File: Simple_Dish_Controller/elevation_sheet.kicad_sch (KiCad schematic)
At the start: 19 parts, among them J2 DA15_Socket, J4 CRJ022-G-TH, Q1 PZT2222A, Q2 PZT2222A, SW2 SW_SPDT_312, U2 74LS08, U3 74LS32, U4 ICM7555xP

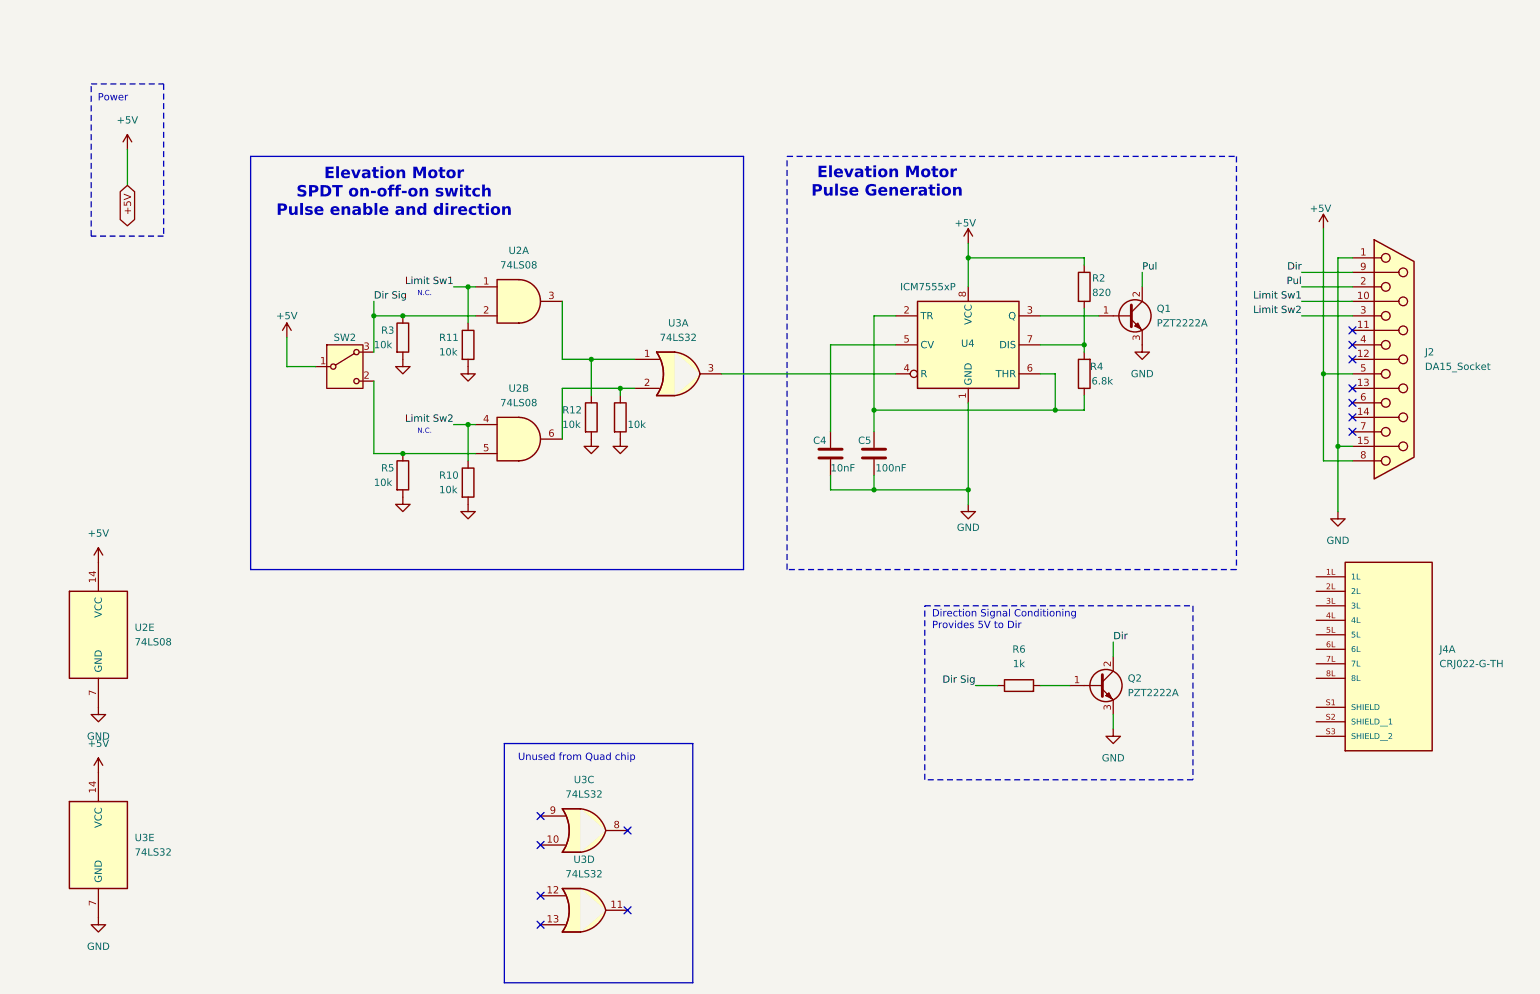
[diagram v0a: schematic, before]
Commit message: Added RJ45 ports
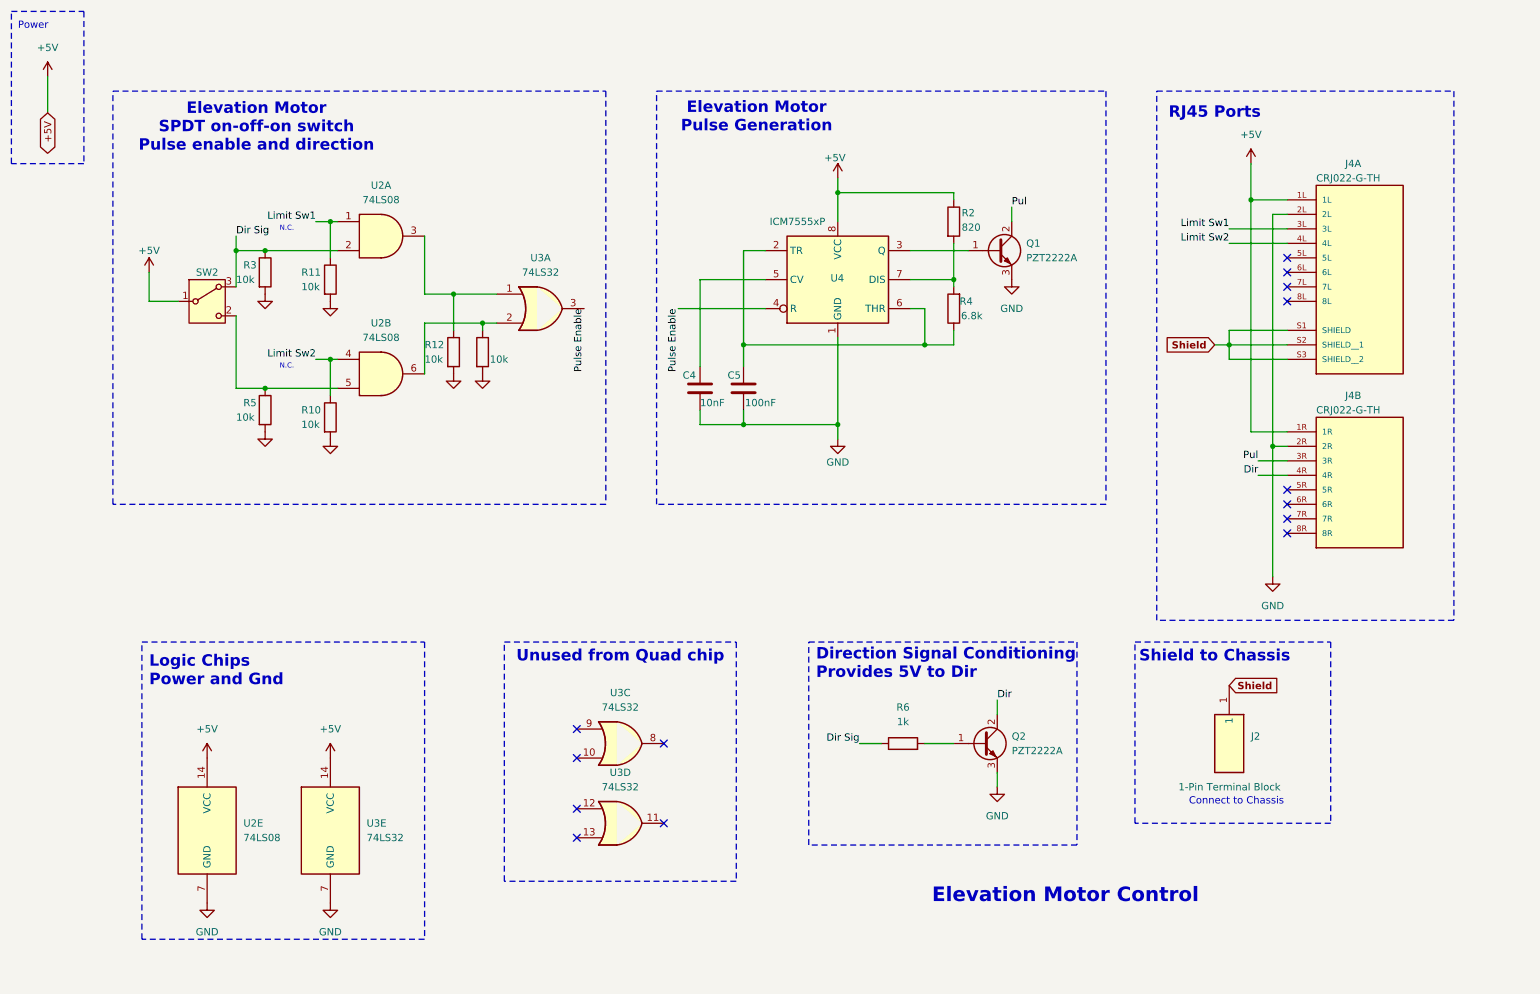
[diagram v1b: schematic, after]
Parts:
- removed J2: DA15_Socket, Connector_Dsub:DSUB-15_Socket_Horizontal_P2.77x2.54mm_EdgePinOffset9.40mm, symbol Connector:DA15_Socket
- added J2: 1-Pin Terminal Block, RHDR1W160P0X826_1X1_1020X1270X1270P, symbol 1-Pin Barrier Terminal Block:38700-6301
- added unit 2 of J4
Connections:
- net +5V: now also J4.1L, J4.1R
- net Dir: now also J4.4R
- net GND: now also J4.2L, J4.2R
- net Limit Sw1: now also J4.3L
- net Limit Sw2: now also J4.4L
- net Pul: now also J4.3R
- net Pulse Enable: now reaches U3.3, U4.4 (R)
- net Shield: now reaches J4.S1 (SHIELD)
- net Shield: now also J4.S2 (SHIELD__1), J4.S3 (SHIELD__2), J2.1
- no-connect marks 13 -> 14
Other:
- note added: "Connect to Chassis"
- note added: "Elevation Motor Control"
- note added: "Logic Chips Power and Gnd"
- note added: "RJ45 Ports"
- note added: "Shield to Chassis"
- moved on the sheet: C4, C5, J4A, Q1, Q2, R10, R11, R12, R2, R3, R4, R5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

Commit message: Footprints defined - passes ERC
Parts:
- J2: footprint RHDR1W160P0X826_1X1_1020X1270X1270P -> 2-port JR45:CUI_CRJ022-G-TH
- J4: footprint CRJ022-G-TH:CUI_CRJ022-G-TH -> 2-port JR45:CUI_CRJ022-G-TH
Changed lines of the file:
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@@
 			)
 		)
-		(property "Footprint" "RHDR1W160P0X826_1X1_1020X1270X1270P"
+		(property "Footprint" "2-port JR45:CUI_CRJ022-G-TH"
 			(at 137.49 151.13 0)
 			(effects
@@
 			)
 		)
-		(property "Footprint" "CRJ022-G-TH:CUI_CRJ022-G-TH"
+		(property "Footprint" "2-port JR45:CUI_CRJ022-G-TH"
 			(at 255.27 97.79 0)
 			(effects
@@
 			)
 		)
-		(property "Footprint" "CRJ022-G-TH:CUI_CRJ022-G-TH"
+		(property "Footprint" "2-port JR45:CUI_CRJ022-G-TH"
 			(at 255.27 59.69 0)
 			(effects

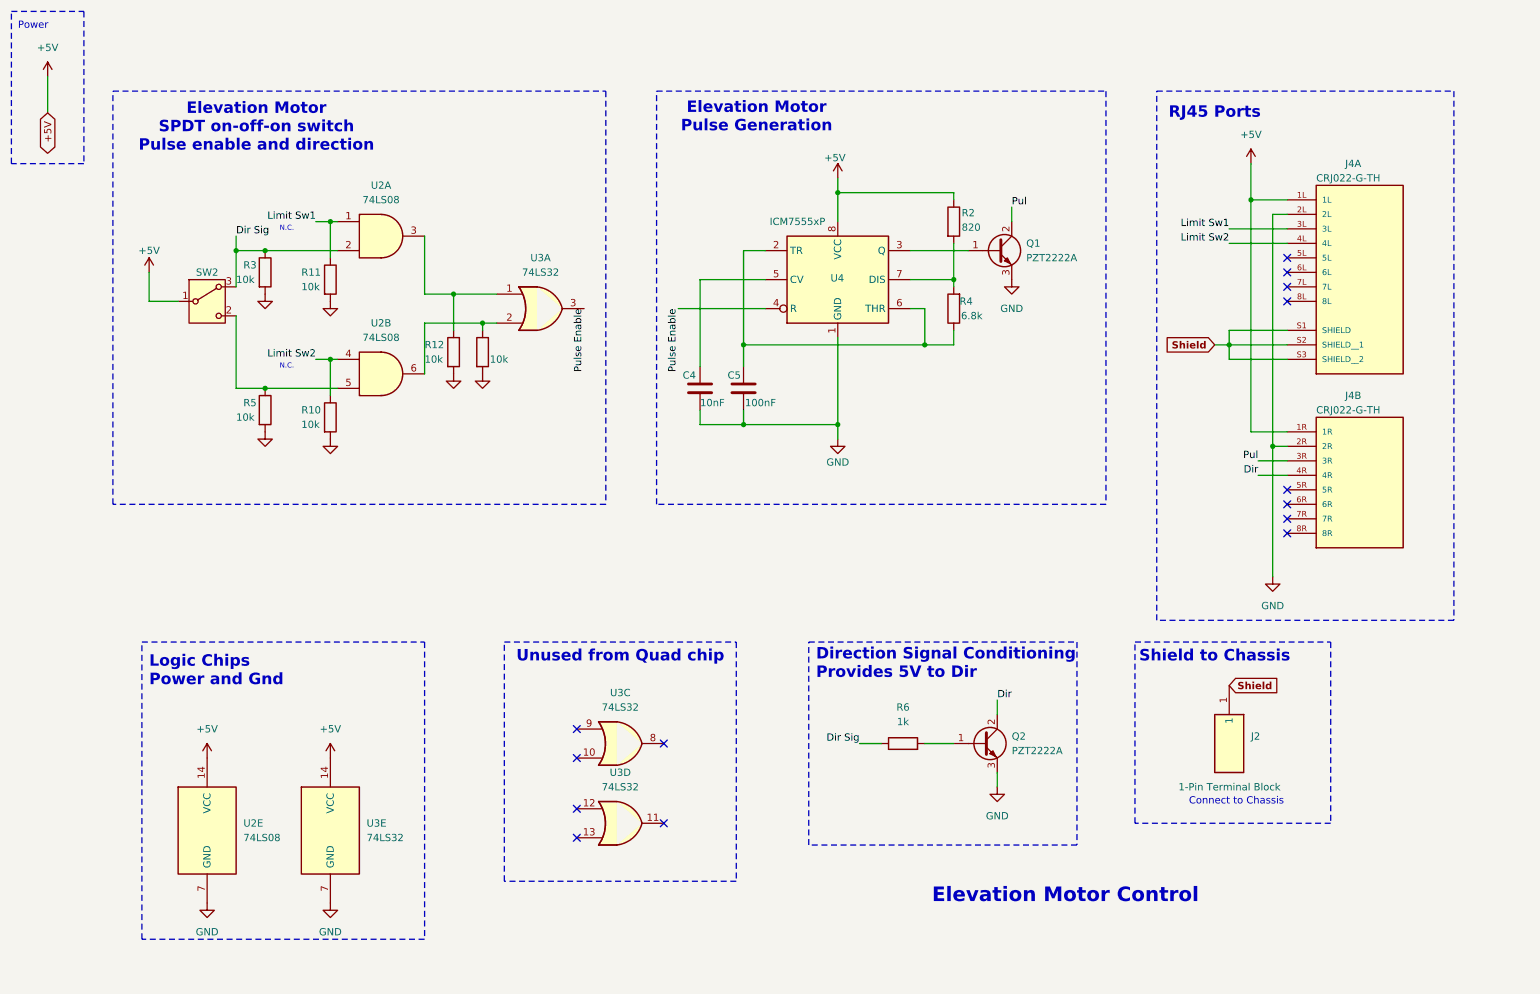
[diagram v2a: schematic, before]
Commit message: 777 chip is now SMD
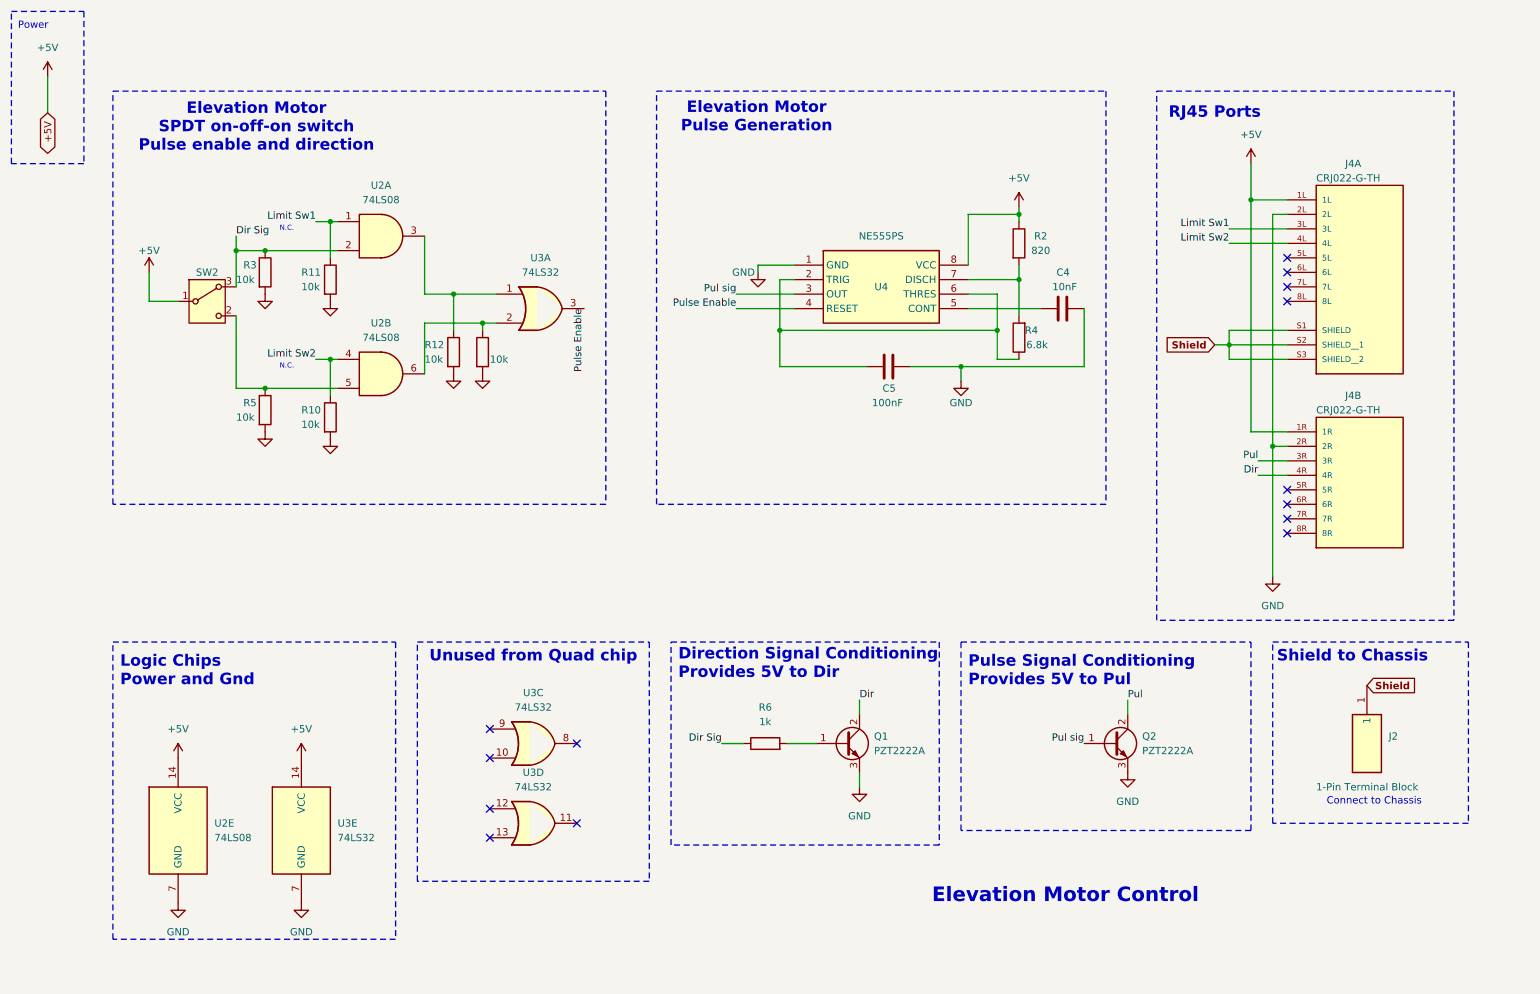
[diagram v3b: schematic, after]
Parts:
- removed Q1: PZT2222A, Package_TO_SOT_SMD:SOT-223-3_TabPin2, symbol Transistor_BJT:PZT2222A
- removed U4: ICM7555xP, Package_SO:SOIC-8_3.9x4.9mm_P1.27mm, symbol Timer:ICM7555xB
- added Q2: PZT2222A, Package_TO_SOT_SMD:SOT-223-3_TabPin2, symbol Transistor_BJT:PZT2222A
- added U4: NE555PS, NE555P Osc Chip SMD:SOIC127P780X200-8N, symbol NE555P Osc Chip SMD:NE555PS
- renumbered Q2 to Q1
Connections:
- net +5V: now also U4.8 (VCC)
- net GND: now also Q2.3 (E), U4.1 (GND)
- net Pul: now also Q2.2 (C)
- net Pulse Enable: now also U4.4 (RESET)
- net at C5.1, R4.1: now also U4.2 (TRIG), U4.6 (THRES)
- net at C4.1: now also U4.5 (CONT)
- net at R2.2, R4.2: now also U4.7 (DISCH)
- new net Pul sig: Q2.1 (B), U4.3 (OUT)
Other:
- note added: "Pulse Signal Conditioning Provides 5V to Pul"
- moved on the sheet: J2, Q1, R6, U2E, U3C, U3D, U3E

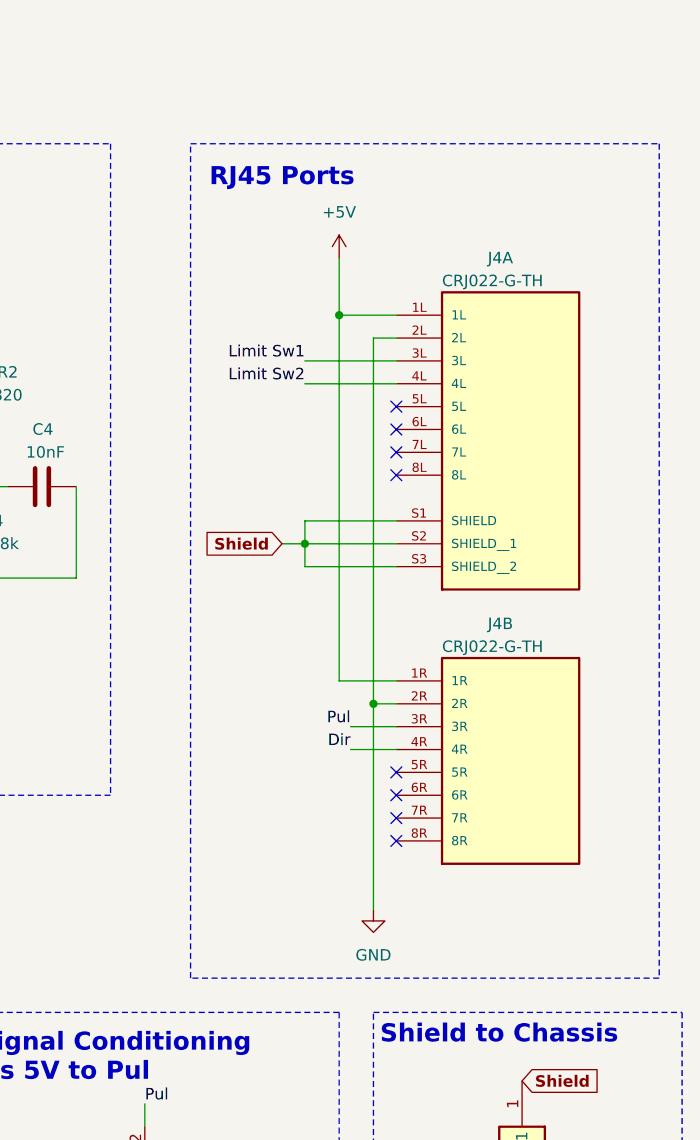
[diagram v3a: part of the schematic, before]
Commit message: Added parts dir
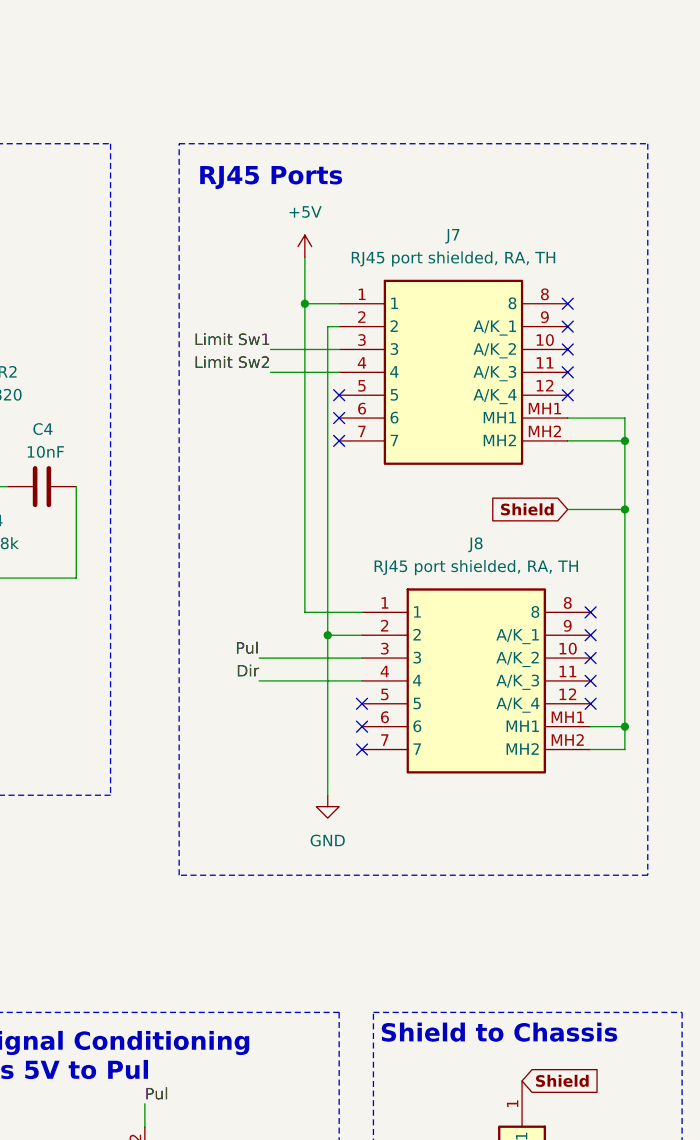
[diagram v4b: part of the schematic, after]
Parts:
- removed J4: CRJ022-G-TH, 2-port JR45:CUI_CRJ022-G-TH, symbol CRJ022-G-TH:CRJ022-G-TH
- added J7, J8: RJ45 port shielded, RA, TH, DishController_footprints:RJ45 Port Shielded, Right Angle TH, symbol DishController_symbols:RJ45 port shielded, Right Angle TH
- C4, C5: footprint (none) -> Capacitor_SMD:C_0805_2012Metric
- J2: footprint 2-port JR45:CUI_CRJ022-G-TH -> 1-Pin Barrier Terminal Block:RHDR1W160P0X826_1X1_1020X1270X1270P
- R10, R11, R12, R13, R2, R3, R4, R5, R6: footprint (none) -> Resistor_SMD:R_0805_2012Metric
- SW2: footprint (none) -> SPDT-90-Deg-On-Off-On:B18JH
- U2: footprint (none) -> 74LS08_SOIC:SOIC127P600X175-14N
- U3: footprint (none) -> 74LS32_SOIC:SOIC127P600X175-14N
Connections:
- net +5V: now also J7.1, J8.1
- net Dir: now also J8.4
- net GND: now also J7.2, J8.2
- net Limit Sw1: now also J7.3
- net Limit Sw2: now also J7.4
- net Pul: now also J8.3
- net Shield: now also J7.MH1, J7.MH2, J8.MH1, J8.MH2
- no-connect marks 14 -> 22
